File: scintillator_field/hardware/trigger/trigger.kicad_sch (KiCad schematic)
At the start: 18 parts, among them U1 OPA855xDSG, U3 TLV3501AIDBV

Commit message: trigger pcb rework
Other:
- added sheet amplifiers (amplifiers.kicad_sch)
- added sheet power (power.kicad_sch)
- added sheet sensors (sensors.kicad_sch)
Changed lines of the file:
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@@
+		)
+	)
+	(sheet
+		(at 68.58 22.86)
+		(size 43.18 29.21)
+		(fields_autoplaced yes)
+		(stroke
+			(width 0.1524)
+			(type solid)
+		)
+		(fill
+			(color 0 0 0 0.0000)
+		)
+		(property "Sheetname" "sensors"
+			(at 68.58 22.1484 0)
+			(effects
+				(font
+					(size 1.27 1.27)
+				)
+				(justify left bottom)
+			)
+		)
+		(property "Sheetfile" "sensors.kicad_sch"
+			(at 68.58 52.6546 0)
+			(effects
+				(font
+					(size 1.27 1.27)
+				)
+				(justify left top)
+			)
+		)
+		(pin "A3" input
+			(at 111.76 41.91 0)
+			(effects
+				(font
+					(size 1.27 1.27)
+				)
+				(justify right)
+			)
+		)
+		(pin "A4" input
+			(at 111.76 44.45 0)
+			(effects
+				(font
+					(size 1.27 1.27)
+				)
+				(justify right)
+			)
+		)
+		(pin "A1" input
+			(at 111.76 36.83 0)
+			(effects
+				(font
+					(size 1.27 1.27)
+				)
+				(justify right)
+			)
+		)
+		(pin "A2" input
+			(at 111.76 39.37 0)
+			(effects
+				(font
+					(size 1.27 1.27)
+				)
+				(justify right)
+			)
+		)
+		(instances
+			(project "trigger"
+				(path "/78398317-4708-4f0b-8983-0fbb7308b4de"
+					(page "3")
+				)
+			)
+		)
+	)
+	(sheet
+		(at 154.94 29.21)
+		(size 31.75 20.32)
+		(fields_autoplaced yes)
+		(stroke
+			(width 0.1524)
+			(type solid)
+		)
+		(fill
+			(color 0 0 0 0.0000)
+		)
+		(property "Sheetname" "amplifiers"
+			(at 154.94 28.4984 0)
+			(effects
+				(font
+					(size 1.27 1.27)
+				)
+				(justify left bottom)
+			)
+		)
+		(property "Sheetfile" "amplifiers.kicad_sch"
+			(at 154.94 50.1146 0)
+			(effects
+				(font
+					(size 1.27 1.27)
+				)
+				(justify left top)
+			)
+		)
+		(instances
+			(project "trigger"
+				(path "/78398317-4708-4f0b-8983-0fbb7308b4de"
+					(page "4")
+				)
+			)
+		)
+	)
+	(sheet
+		(at 26.67 31.75)
+		(size 31.75 29.21)
+		(fields_autoplaced yes)
+		(stroke
+			(width 0.1524)
+			(type solid)
+		)
+		(fill
+			(color 0 0 0 0.0000)
+		)
+		(property "Sheetname" "power"
+			(at 26.67 31.0384 0)
+			(effects
+				(font
+					(size 1.27 1.27)
+				)
+				(justify left bottom)
+			)
+		)
+		(property "Sheetfile" "power.kicad_sch"
+			(at 26.67 61.5446 0)
+			(effects
+				(font
+					(size 1.27 1.27)
+				)
+				(justify left top)
+			)
+		)
+		(instances
+			(project "trigger"
+				(path "/78398317-4708-4f0b-8983-0fbb7308b4de"
+					(page "2")
+				)
+			)
 		)
 	)

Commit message: conclude schematic
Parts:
- removed C10, C12, C2, C4: 1u, Capacitor_SMD:C_0805_2012Metric_Pad1.18x1.45mm_HandSolder, symbol Device:C
- removed C11, C13, C3, C9: 0.1u, Capacitor_SMD:C_0805_2012Metric_Pad1.18x1.45mm_HandSolder, symbol Device:C
- removed C5, C6, C7, C8: 10n, Capacitor_SMD:C_0805_2012Metric_Pad1.18x1.45mm_HandSolder, symbol Device:C
- removed D3: MICROFC-60035-SMT-TR SIPM, sipm:MICROFC-60035-SMT-TR, symbol Device:D_Photo
- removed R5: 49.9R, Resistor_SMD:R_0805_2012Metric_Pad1.20x1.40mm_HandSolder, symbol Device:R
- removed U1: OPA855xDSG, Package_SON:WSON-8-1EP_2x2mm_P0.5mm_EP0.9x1.6mm, symbol Amplifier_Operational:OPA855xDSG
- removed U3: TLV3501AIDBV, Package_TO_SOT_SMD:SOT-23-6, symbol Comparator:TLV3501AIDBV
- added J1, J2, J7, J8: Conn_02x03_Top_Bottom, symbol Connector_Generic:Conn_02x03_Top_Bottom
- added J3, J9: Conn_Coaxial_Small, symbol Connector:Conn_Coaxial_Small
- added J4: A3, symbol Connector:Conn_Coaxial_Small
- added J5: A2, symbol Connector:Conn_Coaxial_Small
- added J6: A1, symbol Connector:Conn_Coaxial_Small
- added R2, R4: 0, Resistor_SMD:R_0805_2012Metric_Pad1.20x1.40mm_HandSolder, symbol Device:R
- added TP1, TP2, TP3, TP4, TP5: TestPoint, symbol Connector:TestPoint
- R1, R3: value 49.9R -> 0
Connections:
- net +5V: now also J1.4 (Pin_4), J2.4 (Pin_4), TP3.1
- net GND: now also J1.1 (Pin_1), J2.1 (Pin_1), J3.2 (Ext), J4.2 (Ext), J5.2 (Ext), J6.2 (Ext), J7.1 (Pin_1), J7.2 (Pin_2), J7.3 (Pin_3), J7.4 (Pin_4), J7.5 (Pin_5), J7.6 (Pin_6), J8.1 (Pin_1), J8.2 (Pin_2), J8.3 (Pin_3), J8.4 (Pin_4), J8.5 (Pin_5), J8.6 (Pin_6), J9.2 (Ext)
- net at R1.2: now also J2.2 (Pin_2)
- net at R3.2: now also J2.6 (Pin_6); no longer R1.1
- net amplifiers/AOUT3: now reaches R3.1
- net amplifiers/AOUT3: now also J4.1 (In)
- new net: J2.3 (Pin_3), R2.2
- new net: J2.5 (Pin_5), R4.2
- new net +2.1V: TP5.1
- new net +3.8V: TP4.1
- new net +33.1V: J9.1 (In), TP2.1
- new net +34.3V: TP1.1
- new net amplifiers/AOUT1: J6.1 (In), R1.1
- new net amplifiers/AOUT2: J5.1 (In), R2.1
- new net amplifiers/AOUT4: J3.1 (In), R4.1
- new net amplifiers/DOUT1: J1.2 (Pin_2)
- new net amplifiers/DOUT2: J1.3 (Pin_3)
- new net amplifiers/DOUT3: J1.6 (Pin_6)
- new net amplifiers/DOUT4: J1.5 (Pin_5)
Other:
- sheet amplifiers ports: added AOUT1, AOUT2, AOUT3, AOUT4, DOUT1, DOUT2, DOUT3, DOUT4, IN1, IN2, IN3, IN4; removed none

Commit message: pcb v1
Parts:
- removed R1, R2, R3, R4: 0, Resistor_SMD:R_0805_2012Metric_Pad1.20x1.40mm_HandSolder, symbol Device:R
- J1, J2, J7, J8: footprint (none) -> connectors:PinHeader_2x03_P2.54mm_Vertical
- J3: renamed from J6; footprint (none) -> connectors:BWIPX-1-001E
- J4: renamed from J5; footprint (none) -> connectors:BWIPX-1-001E
- J5: renamed from J4; footprint (none) -> connectors:BWIPX-1-001E
- J6: renamed from J3; footprint (none) -> connectors:BWIPX-1-001E
- J9: footprint (none) -> connectors:BWIPX-1-001E
- TP1, TP2, TP3, TP4, TP5: footprint (none) -> TestPoint:TestPoint_Pad_D1.0mm
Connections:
- net +5V: now also J2.5 (Pin_5), J2.6 (Pin_6)
- net GND: now also J2.2 (Pin_2), J2.3 (Pin_3)
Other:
- moved on the sheet: J2

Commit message: pcb fabrication files
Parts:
- J3, J4, J5, J6, J9: LCSC (none) -> C496552
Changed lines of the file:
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@@
+			)
+		)
+		(property "LCSC" "C496552"
+			(at 231.14 134.62 0)
+			(effects
+				(font
+					(size 1.27 1.27)
+				)
+				(hide yes)
 			)
 		)
@@
 			)
 		)
+		(property "LCSC" ""
+			(at 180.34 63.5 0)
+			(effects
+				(font
+					(size 1.27 1.27)
+				)
+				(hide yes)
+			)
+		)
 		(pin "1"
 		)
@@
 			)
 		)
+		(property "LCSC" ""
+			(at 175.26 134.62 0)
+			(effects
+				(font
+					(size 1.27 1.27)
+				)
+				(hide yes)
+			)
+		)
 		(pin "1"
 		)
@@
 			)
 		)
+		(property "LCSC" ""
+			(at 114.3 135.89 0)
+			(effects
+				(font
+					(size 1.27 1.27)
+				)
+				(hide yes)
+			)
+		)
 		(pin "1"
 		)
@@
 			)
 		)
+		(property "LCSC" "C496552"
+			(at 195.58 87.63 0)
+			(effects
+				(font
+					(size 1.27 1.27)
+				)
+				(hide yes)
+			)
+		)
 		(pin "2"
 		)
@@
 			)
 		)
+		(property "LCSC" "C496552"
+			(at 182.88 87.63 0)
+			(effects
+				(font
+					(size 1.27 1.27)
+				)
+				(hide yes)
+			)
+		)
 		(pin "2"
 		)
@@
 			)
 		)
+		(property "LCSC" ""
+			(at 214.63 134.62 0)
+			(effects
+				(font
+					(size 1.27 1.27)
+				)
+				(hide yes)
+			)
+		)
 		(pin "1"
 		)
@@
 			)
 		)
+		(property "LCSC" ""
+			(at 91.44 135.89 0)
+			(effects
+				(font
+					(size 1.27 1.27)
+				)
+				(hide yes)
+			)
+		)
 		(pin "1"
 		)
@@
 			)
 		)
+		(property "LCSC" "C496552"
+			(at 176.53 87.63 0)
+			(effects
+				(font
+					(size 1.27 1.27)
+				)
+				(hide yes)
+			)
+		)
 		(pin "2"
 		)
@@
 		)
 		(property "Description" "test point"
+			(at 68.58 135.89 0)
+			(effects
+				(font
+					(size 1.27 1.27)
+				)
+				(hide yes)
+			)
+		)
+		(property "LCSC" ""
 			(at 68.58 135.89 0)
 			(effects
@@
 			)
 		)
+		(property "LCSC" "C496552"
+			(at 189.23 87.63 0)
+			(effects
+				(font
+					(size 1.27 1.27)
+				)
+				(hide yes)
+			)
+		)
 		(pin "2"
 		)
@@
 			)
 		)
+		(property "LCSC" ""
+			(at 80.01 135.89 0)
+			(effects
+				(font
+					(size 1.27 1.27)
+				)
+				(hide yes)
+			)
+		)
 		(pin "1"
 		)
@@
 		)
 		(property "Description" "test point"
+			(at 102.87 135.89 0)
+			(effects
+				(font
+					(size 1.27 1.27)
+				)
+				(hide yes)
+			)
+		)
+		(property "LCSC" ""
 			(at 102.87 135.89 0)
 			(effects
@@
 			(at 194.31 134.62 0)
 			(effects
+				(font
+					(size 1.27 1.27)
+				)
+				(hide yes)
+			)
+		)
+		(property "LCSC" ""
+			(at 194.31 134.62 0)
+			(effects

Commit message: fix trigger pcb
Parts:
- added J10, J11, J12, J13: Conn_Coaxial_Small, connectors:BWIPX-1-001E, symbol Connector:Conn_Coaxial_Small
- J3: value A1 -> Conn_Coaxial_Small
- J4: value A2 -> Conn_Coaxial_Small
- J5: value A3 -> Conn_Coaxial_Small
- renumbered TP5 to +1V2, TP2 to +33V1, TP1 to +34V3, TP4 to +3V8, TP3 to +5V0
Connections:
- net GND: now also J10.2 (Ext), J11.2 (Ext), J12.2 (Ext), J13.2 (Ext)
- net amplifiers/DOUT1: now also J10.1 (In)
- net amplifiers/DOUT2: now also J11.1 (In)
- net amplifiers/DOUT3: now also J12.1 (In)
- net amplifiers/DOUT4: now also J13.1 (In)
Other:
- moved on the sheet: J1

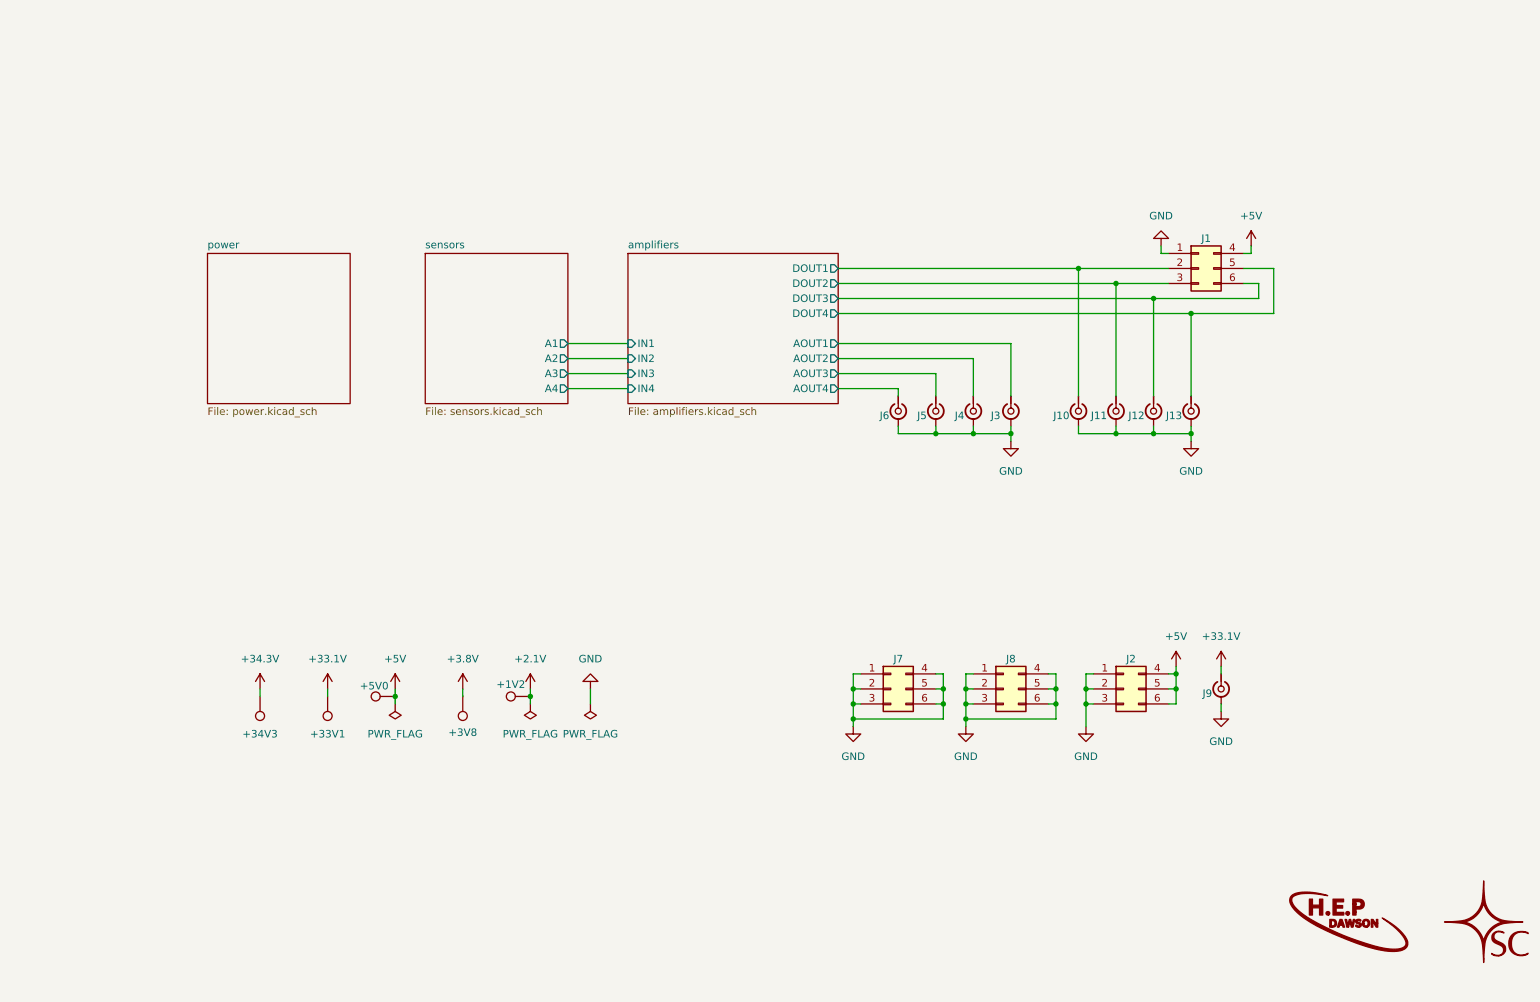
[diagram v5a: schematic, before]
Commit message: update to opa858
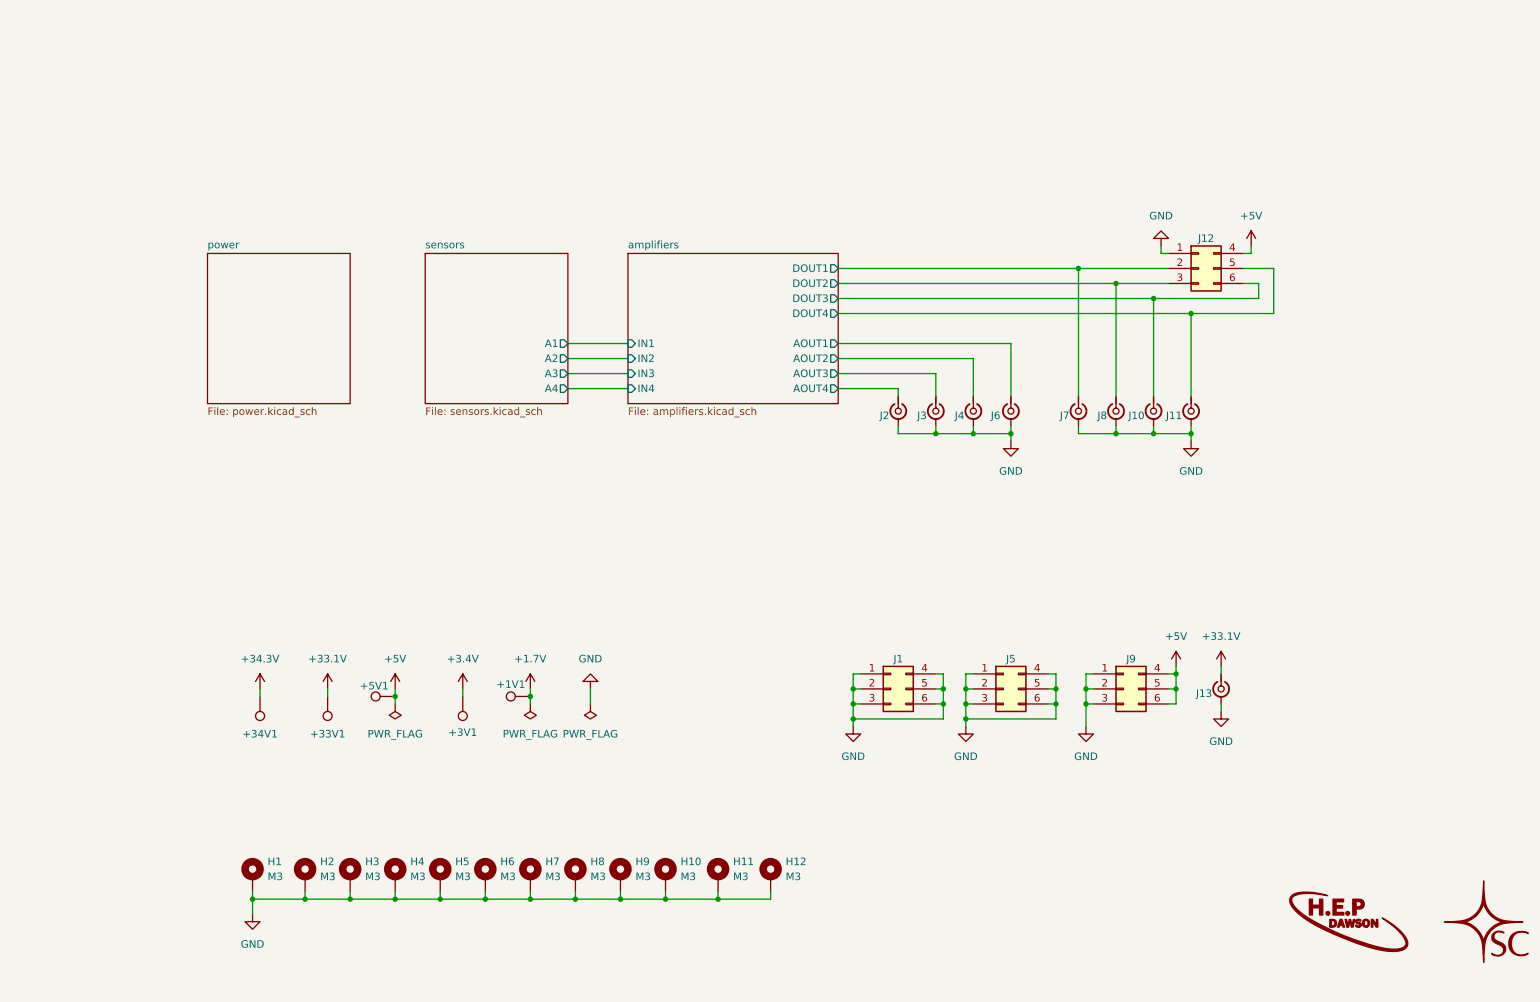
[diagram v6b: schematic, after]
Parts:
- added H1, H10, H11, H12, H2, H3, H4, H5, H6, H7, H8, H9: M3, MountingHole:MountingHole_3.2mm_M3_DIN965_Pad, symbol Mechanical:MountingHole_Pad
- renumbered +1V2 to +1V1, +34V3 to +34V1, +3V8 to +3V1, +5V0 to +5V1, J7 to J1, J12 to J10, J13 to J11, J1 to J12, J9 to J13, J6 to J2, J5 to J3, J8 to J5, J3 to J6, J10 to J7, J11 to J8, J2 to J9
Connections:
- net GND: now also H1.1, H10.1, H11.1, H12.1, H2.1, H3.1, H4.1, H5.1, H6.1, H7.1, H8.1, H9.1
- net +2.1V renamed +1.7V
- net +3.8V renamed +3.4V

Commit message: refactor hardware
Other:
- company: Alex Xia -> (none)
- title: Scintillating Chamber: SIPM Amplifier -> Scintillating Chamber: SIPM Trigger Board
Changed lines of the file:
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@@
 	(paper "A4")
 	(title_block
-		(title "Scintillating Chamber: SIPM Amplifier")
+		(title "Scintillating Chamber: SIPM Trigger Board")
 		(date "2025-03-11")
-		(rev "2")
-		(company "Alex Xia")
+		(rev "3")
+		(comment 3 "Dawson Enriched Pure & Applied")
+		(comment 4 "Alex Xia")
 	)
 	(junction
